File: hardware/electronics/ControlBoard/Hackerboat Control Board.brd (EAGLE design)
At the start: 177.8 x 114.3 mm, 178 parts, among them J3 3-1437664-0, U1 IPS6044, U14 TPS54331, U15 TPS54331, U2 ARDUINO-MEGAFULL, U3 IPS6044, U4 IPS6044, U5 IPS6044

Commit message: Added hardware test code Various modifications to 'as-built' condition Added TODO.md
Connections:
- net N$1 renamed GNSS_RX
- net N$2 renamed GNSS_TX
- net N$67 renamed SYS_5V
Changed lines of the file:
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@@
 <wire x1="54.61" y1="60.325" x2="56.515" y2="58.42" width="0.254" layer="1"/>
 </signal>
-<signal name="N$1">
+<signal name="GNSS_RX">
 <contactref element="GPS" pad="RX"/>
 <contactref element="U$1" pad="59"/>
@@
 <wire x1="57.785" y1="49.53" x2="59.055" y2="48.26" width="0.254" layer="16"/>
 </signal>
-<signal name="N$2">
+<signal name="GNSS_TX">
 <contactref element="GPS" pad="TX"/>
 <contactref element="U$1" pad="57"/>
@@
 <wire x1="59.055" y1="43.18" x2="63.373" y2="43.18" width="0.4064" layer="16"/>
 </signal>
-<signal name="N$67">
+<signal name="SYS_5V">
 <contactref element="GPS" pad="VIN"/>
 <contactref element="U$1" pad="53"/>

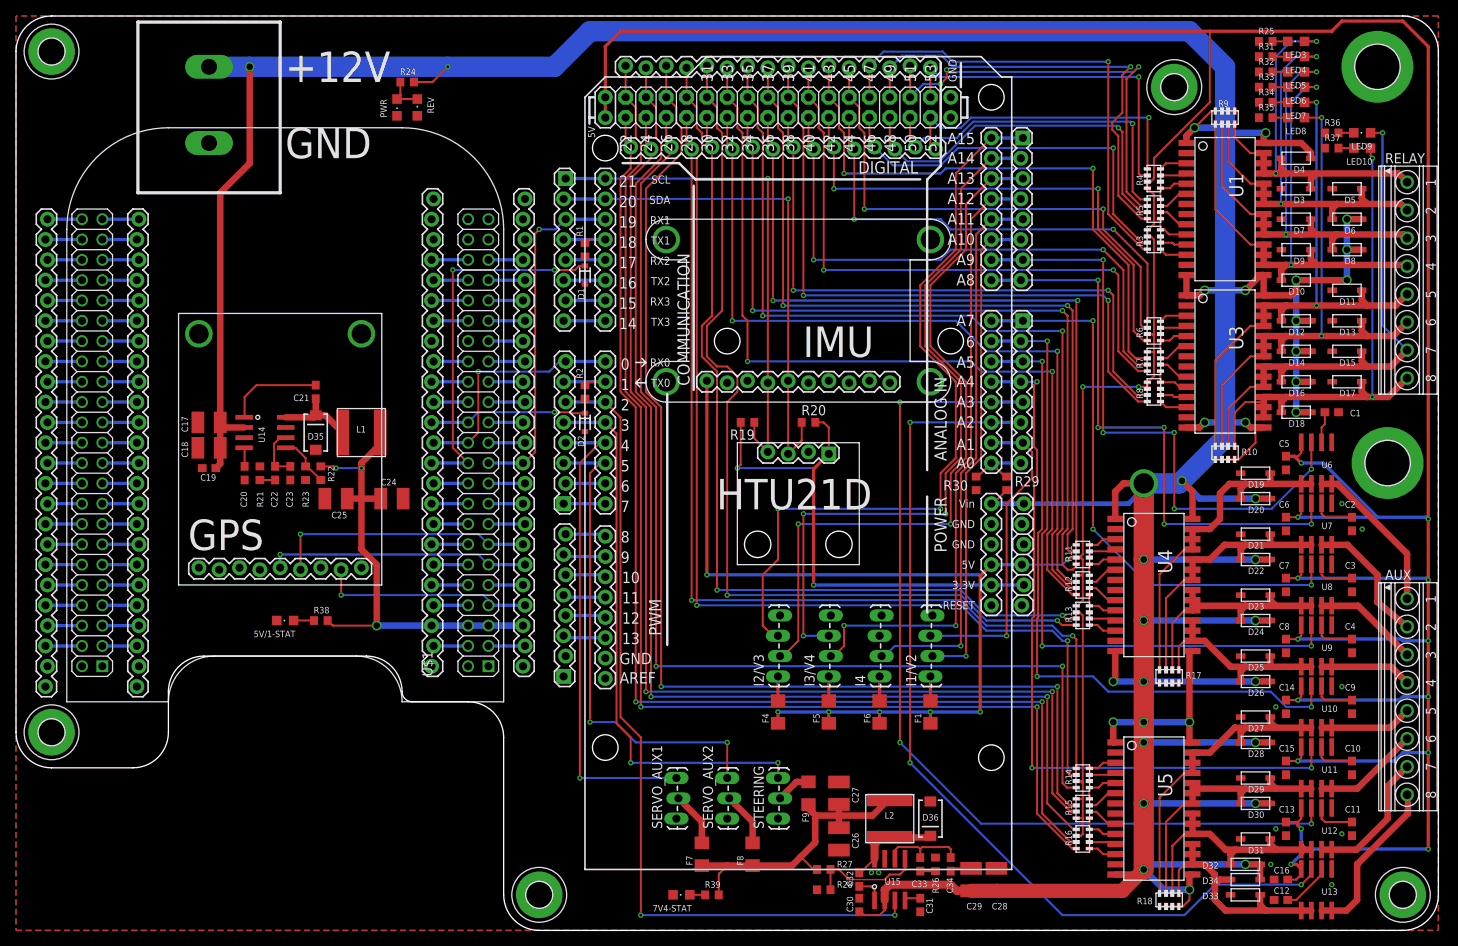
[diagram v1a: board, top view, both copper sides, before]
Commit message: Initial trimming of unnecessary parts in preparation for serious work. Keeping the power supply circuits, BBB connection, IMU, and GPS.
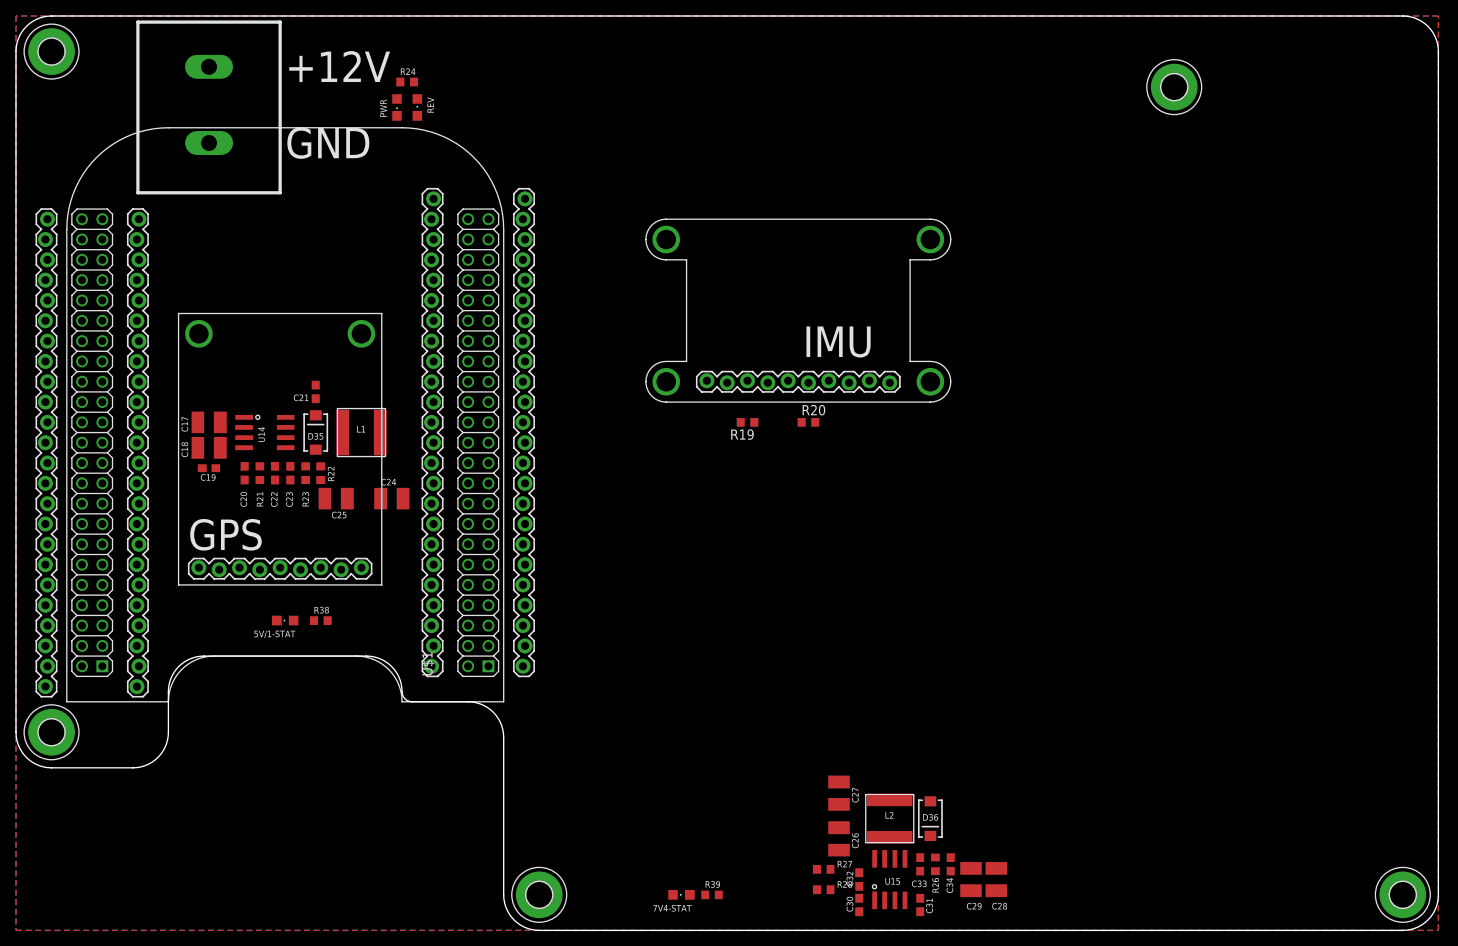
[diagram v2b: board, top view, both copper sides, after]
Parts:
- removed AUX, RELAY: 1751303, con-phoenix-350:1751303
- removed C1, C10, C11, C12, C2, C3, C4, C9: 1n, resistor:C0603
- removed C13, C14, C15, C16, C5, C6, C7, C8: 100n, resistor:C0603
- removed D1, D2: 3.3V, SparkFun-DiscreteSemi:SOD-323
- removed D10, D11, D12, D13, D14, D15, D16, D17, D18, D19, D20, D21, D22, D23, D24, D25, D26, D27, D28, D29, D3, D30, D31, D32, D33, D34, D4, D5, D6, D7, D8, D9: (no value), adafruit:SOD-123
- removed F1, F4, F5, F6, F7, F8, F9: (no value), adafruit:R1206
- removed H5, H6: MOUNT-PAD-ROUND5.5, holes:5,5-PAD
- removed HTU21D: HTU21D, sparkfun-sensor-boards:HTU21D
- removed I1/V2, I2/V3, I3/V4, I4: (no value), SparkFun-Connectors:1X04_LOCK_LONGPADS
- removed JP10, JP11, JP12, JP13, JP14: (no value), SparkFun-Connectors:1X08_LOCK
- removed JP15, JP16: M16LOCK, SparkFun-Connectors:1X16_LOCK
- removed JP17: (no value), SparkFun-Connectors:1X06_LOCK
- removed LED10, LED3, LED4, LED5, LED6, LED7, LED8, LED9: (no value), adafruit:CHIPLED_0805
- removed R1, R2: 1K, resistor:R0603
- removed R10, R17, R18, R9: 100K, res-cap-arrays:CTS742C083-RES
- removed R11, R12, R13, R14, R15, R16, R3, R5, R6, R7, R8: 10K, res-cap-arrays:CTS742C083-RES
- removed R25, R31, R32, R33, R34, R35, R36, R37: (no value), resistor:R0603
- removed R29: 15K, resistor:R0603
- removed R30: 10K, resistor:R0603
- removed R4: 10k, res-cap-arrays:CTS742C083-RES
- removed SERVO_AUX1, SERVO_AUX2, STEERING: (no value), SparkFun-Connectors:1X03_LOCK_LONGPADS
- removed U1, U3, U4, U5: IPS6044, logos-faves:SO-28L
- removed U10, U11, U12, U13, U6, U7, U8, U9: (no value), allegro3:SO08
- removed U2: ARDUINO-MEGAFULL, SparkFun-Boards:ARDUINO_MEGA
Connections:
- removed net +5V/1: C24.1, C25.1, L1.2, R22.2, R38.2, U$1.51, U$1.52, U$2.23, U$5.23
- removed net 13: JP14.3, U2.13
- removed net AUX1: JP15.9, R11.1, U2.36
- removed net AUX1FB: JP16.9, R11.3, U2.37
- removed net AUX1I: JP12.7, U2.A9, U6.7
- removed net AUX2: JP16.10, R12.3, U2.35
- removed net AUX2FB: JP15.10, R11.7, U2.34
- removed net AUX2I: JP12.8, U2.A8, U7.7
- removed net AUX3: JP15.11, R12.5, U2.32
- removed net AUX3FB: JP16.11, R12.7, U2.33
- removed net AUX3I: JP11.1, U2.A7, U8.7
- removed net AUX4: JP16.12, R13.7, U2.31
- removed net AUX4FB: JP15.12, R13.5, U2.30
- removed net AUX4I: JP11.2, U2.A6, U9.7
- removed net AUX5: JP15.13, R14.1, U2.28
- removed net AUX5FB: JP16.13, R14.3, U2.29
- removed net AUX5I: JP11.3, U10.7, U2.A5
- removed net AUX6: JP16.14, R15.3, U2.27
- removed net AUX6FB: JP15.14, R14.7, U2.26
- removed net AUX6I: JP11.4, U11.7, U2.A4
- removed net AUX7: JP15.15, R15.5, U2.24
- removed net AUX7FB: JP16.15, R16.1, U2.25
- removed net AUX7I: JP11.5, U12.7, U2.A3
- removed net AUX8: JP16.16, R16.7, U2.23
- removed net AUX8FB: JP15.16, R16.5, U2.22
- removed net AUX8I: JP11.6, U13.7, U2.A2
- removed net I1: I1/V2.2, JP12.6, U2.A10
- removed net I2: I2/V3.2, JP12.3, U2.A13
- removed net I3: I3/V4.2, JP12.4, U2.A12
- removed net I4: I4.2, JP12.5, U2.A11
- removed net N$10: D7.C, D8.A, LED5.A, R9.3, RELAY.3, U1.19, U1.20, U1.21
- removed net N$100: JP14.7, U2.9
- removed net N$101: JP14.6, U2.10
- removed net N$102: JP14.5, U2.11
- removed net N$103: JP14.4, U2.12
- removed net N$11: D10.A, D9.C, LED6.A, R9.1, RELAY.4, U1.16, U1.17, U1.18
- removed net N$12: R4.2, U1.3
- removed net N$13: R5.4, U1.6
- removed net N$14: R5.6, U1.9
- removed net N$15: R3.8, U1.12
- removed net N$16: R4.4, R4.6, U1.4
- removed net N$17: R4.8, R5.2, U1.5
- removed net N$178: LED3.C, R25.2
- removed net N$179: LED4.C, R31.2
- removed net N$18: R3.2, R5.8, U1.10
- removed net N$180: LED5.C, R32.2
- removed net N$181: LED6.C, R33.2
- removed net N$186: LED7.C, R34.2
- removed net N$187: LED8.C, R35.2
- removed net N$188: LED9.C, R36.2
- removed net N$189: LED10.C, R37.2
- removed net N$19: R3.4, R3.6, U1.11
- removed net N$20: R7.4, U3.6
- removed net N$21: R6.8, R7.2, U3.5
- removed net N$22: R6.4, R6.6, U3.4
- removed net N$23: R7.8, R8.2, U3.10
- removed net N$24: R8.4, R8.6, U3.11
- removed net N$25: D11.C, D12.A, LED7.A, R10.7, RELAY.5, U3.25, U3.26, U3.27
- removed net N$26: D13.C, D14.A, LED8.A, R10.5, RELAY.6, U3.22, U3.23, U3.24
- removed net N$27: D15.C, D16.A, LED9.A, R10.3, RELAY.7, U3.19, U3.20, U3.21
- removed net N$28: D17.C, D18.A, LED10.A, R10.1, RELAY.8, U3.16, U3.17, U3.18
- removed net N$29: D25.C, D26.A, R17.1, U4.16, U4.17, U4.18, U9.1, U9.2
- removed net N$3: JP13.4, R1.1, U2.18
- removed net N$30: AUX.2, U7.3, U7.4
- removed net N$31: AUX.3, U8.3, U8.4
- removed net N$32: AUX.4, U9.3, U9.4
- removed net N$33: AUX.5, U10.3, U10.4
- removed net N$34: D19.C, D20.A, R17.7, U4.25, U4.26, U4.27, U6.1, U6.2
- removed net N$35: D21.C, D22.A, R17.5, U4.22, U4.23, U4.24, U7.1, U7.2
- removed net N$36: D23.C, D24.A, R17.3, U4.19, U4.20, U4.21, U8.1, U8.2
- removed net N$37: AUX.1, U6.3, U6.4
- removed net N$38: R11.2, U4.3
- removed net N$39: R12.4, U4.6
- removed net N$4: JP10.7, R2.2, U2.1
- removed net N$40: R12.6, U4.9
- removed net N$41: R13.8, U4.12
- removed net N$42: R11.4, R11.6, U4.4
- removed net N$43: R11.8, R12.2, U4.5
- removed net N$44: R12.8, R13.2, U4.10
- removed net N$45: R13.4, R13.6, U4.11
- removed net N$46: R14.2, U5.3
- removed net N$47: R16.8, U5.12
- removed net N$48: R15.6, U5.9
- removed net N$49: R15.4, U5.6
- removed net N$5: R6.2, U3.3
- removed net N$50: R14.4, R14.6, U5.4
- removed net N$51: R14.8, R15.2, U5.5
- removed net N$52: R15.8, R16.2, U5.10
- removed net N$53: R16.4, R16.6, U5.11
- removed net N$54: D27.C, D28.A, R18.7, U10.1, U10.2, U5.25, U5.26, U5.27
- removed net N$55: D29.C, D30.A, R18.5, U11.1, U11.2, U5.22, U5.23, U5.24
- removed net N$56: D31.C, D32.A, R18.3, U12.1, U12.2, U5.19, U5.20, U5.21
- removed net N$57: D33.C, D34.A, R18.1, U13.1, U13.2, U5.16, U5.17, U5.18
- removed net N$58: AUX.6, U11.3, U11.4
- removed net N$59: AUX.7, U12.3, U12.4
- removed net N$6: R8.8, U3.12
- removed net N$60: AUX.8, U13.3, U13.4
- removed net N$61: C1.2, U6.6
- removed net N$64: C2.2, U7.6
- removed net N$65: C3.2, U8.6
- removed net N$66: C4.2, U9.6
- removed net N$7: R7.6, U3.9
- removed net N$74: C9.2, U10.6
- removed net N$75: C10.2, U11.6
- removed net N$76: C11.2, U12.6
- removed net N$77: C12.2, U13.6
- removed net N$8: D3.C, D4.A, LED3.A, R9.7, RELAY.1, U1.25, U1.26, U1.27
- removed net N$83: F1.2, I1/V2.1
- removed net N$86: F4.2, I2/V3.1
- removed net N$87: F5.2, I3/V4.1
- removed net N$88: F6.2, I4.1
- removed net N$89: F7.2, SERVO_AUX1.2
- removed net N$9: D5.C, D6.A, LED4.A, R9.5, RELAY.2, U1.22, U1.23, U1.24
- removed net N$90: F8.2, SERVO_AUX2.2
- removed net N$91: JP10.1, U2.7
- removed net N$92: JP10.2, U2.6
- removed net N$93: F9.2, STEERING.2
- removed net N$94: JP11.8, R29.1, R30.2, U2.A0
- removed net N$95: JP13.5, U2.17
- removed net N$96: JP13.6, U2.16
- removed net N$97: JP13.7, U2.15
- removed net N$98: JP13.8, U2.14
- removed net N$99: JP14.8, U2.8
- removed net RELAY1: JP15.1, R4.1, U2.52
- removed net RELAY1FB: JP16.1, R4.3, U2.53
- removed net RELAY2: JP16.2, R5.3, U2.51
- removed net RELAY2FB: JP15.2, R5.1, U2.50
- removed net RELAY3: JP15.3, R5.5, U2.48
- removed net RELAY3FB: JP16.3, R5.7, U2.49
- removed net RELAY4: JP16.4, R3.7, U2.47
- removed net RELAY4FB: JP15.4, R3.5, U2.46
- removed net RELAY5: JP15.5, R6.1, U2.44
- removed net RELAY5FB: JP16.5, R6.3, U2.45
- removed net RELAY6: JP16.6, R7.3, U2.43
- removed net RELAY6FB: JP15.6, R6.7, U2.42
- removed net RELAY7: JP15.7, R7.5, U2.40
- removed net RELAY7FB: JP16.7, R7.7, U2.41
- removed net RELAY8: JP16.8, R8.7, U2.39
- removed net RELAY8FB: JP15.8, R8.5, U2.38
- removed net SCL: HTU21D.SCL, IMU.SCL, JP13.1, R19.1, U2.21
- removed net SDA: HTU21D.SDA, IMU.SDA, JP13.2, R20.1, U2.20
- removed net SERVO_AUX1: JP10.4, SERVO_AUX1.3, U2.4
- removed net SERVO_AUX2: JP10.3, SERVO_AUX2.3, U2.5
- removed net STEERING: JP10.5, STEERING.3, U2.3
- removed net V2: I1/V2.3, JP11.7, U2.A1
- removed net V3: I2/V3.3, JP12.1, U2.A15
- removed net V4: I3/V4.3, JP12.2, U2.A14
- new net N$196: IMU.SDA, R20.1
- new net N$197: IMU.SCL, R19.1
- net +12V: no longer D10.C, D12.C, D14.C, D16.C, D18.C, D20.C, D22.C, D24.C, D26.C, D28.C, D30.C, D32.C, D34.C, D4.C, D6.C, D8.C, JP17.6, R10.2, R10.4, R10.6, R10.8, R17.2, R17.4, R17.6, R17.8, R18.2, R18.4, R18.6, R18.8, R29.2, R9.2, R9.4, R9.6, R9.8, U1.1, U1.14, U1.15, U1.28, U2.VIN, U3.1, U3.14, U3.15, U3.28, U4.1, U4.14, U4.15, U4.28, U5.1, U5.14, U5.15, U5.28
- net +3V3: no longer HTU21D.3V3, JP17.2, U2.3.3V
- net +5V: now also C24.1, C25.1, L1.2, R22.2, R38.2, U$1.51, U$1.52, U$2.23, U$5.23; no longer C13.2, C14.2, C15.2, C16.2, C5.2, C6.2, C7.2, C8.2, F1.1, F4.1, F5.1, F6.1, JP17.3, R11.5, R12.1, R13.1, R13.3, R14.5, R15.1, R15.7, R16.3, R3.1, R3.3, R4.5, R4.7, R6.5, R7.1, R8.1, R8.3, U10.8, U11.8, U12.8, U13.8, U2.5V@0, U2.5V@1, U2.5V@2, U6.8, U7.8, U8.8, U9.8
- net 7V4: no longer F7.1, F8.1, F9.1
- net GND: no longer C1.1, C10.1, C11.1, C12.1, C13.1, C14.1, C15.1, C16.1, C2.1, C3.1, C4.1, C5.1, C6.1, C7.1, C8.1, C9.1, D1.A, D11.A, D13.A, D15.A, D17.A, D19.A, D2.A, D21.A, D23.A, D25.A, D27.A, D29.A, D3.A, D31.A, D33.A, D5.A, D7.A, D9.A, H5.B5,5, H6.B5,5, HTU21D.GND, I1/V2.4, I2/V3.4, I3/V4.4, I4.4, JP17.4, JP17.5, R25.1, R30.1, R31.1, R32.1, R33.1, R34.1, R35.1, R36.1, R37.1, SERVO_AUX1.1, SERVO_AUX2.1, STEERING.1, U1.13, U1.2, U1.7, U1.8, U10.5, U11.5, U12.5, U13.5, U2.GND@0, U2.GND@1, U2.GND@2, U2.GND@3, U2.GND@4, U3.13, U3.2, U3.7, U3.8, U4.13, U4.2, U4.7, U4.8, U5.13, U5.2, U5.7, U5.8, U6.5, U7.5, U8.5, U9.5
- net RX0: no longer JP10.8, U2.0
- net RX1: no longer JP13.3, U2.19
- net SERVO_EN: no longer JP10.6, U2.2
- net TX0: no longer D2.C, R2.1
- net TX1: no longer D1.C, R1.2
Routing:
- net +12V: track 644.3 -> 0.00 mm, vias 36 -> 0
- net +5V: track 604.3 -> 0.00 mm, vias 23 -> 0
- net AUX8: track 152.1 -> 0.00 mm, vias 2 -> 0
- net AUX7FB: track 149.4 -> 0.00 mm, vias 2 -> 0
- net AUX6: track 146.9 -> 0.00 mm, vias 2 -> 0
- net AUX8FB: track 145.1 -> 0.00 mm, vias 2 -> 0
- net AUX7: track 141.3 -> 0.00 mm, vias 2 -> 0
- net AUX6FB: track 138.6 -> 0.00 mm, vias 2 -> 0
- net AUX5FB: track 134.1 -> 0.00 mm, vias 2 -> 0
- net AUX5: track 126.8 -> 0.00 mm, vias 2 -> 0
- net AUX8I: track 117.2 -> 0.00 mm, vias 3 -> 0
- net AUX4: track 115.8 -> 0.00 mm, vias 2 -> 0
- net AUX7I: track 115.5 -> 0.00 mm, vias 3 -> 0
- net AUX4FB: track 107.0 -> 0.00 mm, vias 2 -> 0
- net AUX3FB: track 106.3 -> 0.00 mm, vias 2 -> 0
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
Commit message: First cut at the system block diagram
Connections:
- removed net N$118: U$1.50, U$2.24
- removed net N$71: U$1.49, U$5.24
- net +3V3: now also U$1.49, U$1.50, U$2.24, U$5.24
- net GND: no longer GPS.GND
- net GNSS_RX: no longer GPS.RX
- net GNSS_TX: no longer GPS.TX
- net SYS_5V: no longer GPS.VIN
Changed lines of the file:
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@@
 <contactref element="U$1" pad="91"/>
 <contactref element="U$1" pad="89"/>
-<contactref element="U$1" pad="92"/>
 <contactref element="U$1" pad="90"/>
-<contactref element="U$1" pad="2"/>
-<contactref element="U$1" pad="48"/>
-<contactref element="U$1" pad="80"/>
 <contactref element="IMU" pad="GND"/>
 <contactref element="H1" pad="B3,2"/>
@@
 <contactref element="C27" pad="2"/>
 <contactref element="R28" pad="1"/>
-<contactref element="U$2" pad="3"/>
 <contactref element="U$2" pad="4"/>
-<contactref element="U$2" pad="9"/>
-<contactref element="U$2" pad="25"/>
-<contactref element="U$3" pad="24"/>
 <contactref element="U$5" pad="4"/>
 <contactref element="J3" pad="2"/>
@@
 <contactref element="U$1" pad="1"/>
 <contactref element="U$1" pad="47"/>
-<contactref element="GPS" pad="GND"/>
 <contactref element="U$4" pad="24"/>
 <contactref element="U$5" pad="25"/>
@@
 <contactref element="7V4-STAT" pad="C"/>
 <contactref element="H7" pad="B3,2"/>
+<contactref element="U$1" pad="92"/>
+<contactref element="U$1" pad="92"/>
+<contactref element="U$2" pad="3"/>
+<contactref element="U$1" pad="2"/>
+<contactref element="U$1" pad="48"/>
+<contactref element="U$2" pad="25"/>
+<contactref element="U$3" pad="24"/>
+<contactref element="U$1" pad="80"/>
+<contactref element="U$2" pad="9"/>
 <wire x1="114.3" y1="86.36" x2="144.78" y2="105.41" width="0" layer="19" extent="1-1"/>
 <wire x1="114.3" y1="68.58" x2="114.3" y2="86.36" width="0" layer="19" extent="1-1"/>
@@
 <wire x1="22.73" y1="60.325" x2="23.28" y2="57.785" width="0" layer="19" extent="1-1"/>
 <wire x1="22.73" y1="63.5" x2="22.73" y2="60.325" width="0" layer="19" extent="1-1"/>
-<wire x1="38.1" y1="45.339" x2="38.605" y2="53.975" width="0" layer="19" extent="1-1"/>
-<wire x1="32.605" y1="38.735" x2="38.1" y2="45.339" width="0" layer="19" extent="1-1"/>
 <wire x1="48.39" y1="53.975" x2="38.605" y2="53.975" width="0" layer="19" extent="1-1"/>
 <wire x1="22.86" y1="74.5744" x2="22.73" y2="63.5" width="0" layer="19" extent="1-1"/>
+<wire x1="32.605" y1="38.735" x2="38.605" y2="53.975" width="0" layer="19" extent="1-1"/>
 <wire x1="15.367" y1="33.02" x2="32.605" y2="38.735" width="0" layer="19" extent="1-1"/>
 <wire x1="10.795" y1="33.02" x2="15.367" y2="33.02" width="0" layer="19" extent="1-1"/>
@@
 <wire x1="3.937" y1="33.02" x2="8.255" y2="33.02" width="0" layer="19" extent="1-1"/>
 <wire x1="4.445" y1="24.765" x2="3.937" y2="33.02" width="0" layer="19" extent="1-1"/>
-<wire x1="51.943" y1="33.02" x2="38.1" y2="45.339" width="0" layer="19" extent="1-1"/>
+<wire x1="51.943" y1="33.02" x2="32.605" y2="38.735" width="0" layer="19" extent="1-1"/>
 <wire x1="56.515" y1="33.02" x2="51.943" y2="33.02" width="0" layer="19" extent="1-1"/>
 <wire x1="59.055" y1="33.02" x2="56.515" y2="33.02" width="0" layer="19" extent="1-1"/>
@@
 </signal>
 <signal name="GNSS_RX">
-<contactref element="GPS" pad="RX"/>
 <contactref element="U$1" pad="59"/>
 <contactref element="U$5" pad="19"/>
 <wire x1="59.055" y1="48.26" x2="63.373" y2="48.26" width="0" layer="19" extent="1-1"/>
-<wire x1="35.56" y1="45.085" x2="59.055" y2="48.26" width="0" layer="19" extent="1-1"/>
 </signal>
 <signal name="GNSS_TX">
-<contactref element="GPS" pad="TX"/>
 <contactref element="U$1" pad="57"/>
 <contactref element="U$5" pad="20"/>
 <wire x1="59.055" y1="45.72" x2="63.627" y2="45.72" width="0" layer="19" extent="1-1"/>
-<wire x1="33.02" y1="45.339" x2="59.055" y2="45.72" width="0" layer="19" extent="1-1"/>
 </signal>
 <signal name="+3V3">
 <contactref element="R19" pad="2"/>
 <contactref element="R20" pad="2"/>
+<contactref element="U$1" pad="49"/>
+<contactref element="U$5" pad="24"/>
+<contactref element="U$1" pad="50"/>
+<contactref element="U$2" pad="24"/>
 <wire x1="90.59" y1="63.5" x2="99.91" y2="63.5" width="0" layer="19" extent="1-1"/>
+<wire x1="63.627" y1="35.56" x2="90.59" y2="63.5" width="0" layer="19" extent="1-1"/>
+<wire x1="59.055" y1="35.56" x2="63.627" y2="35.56" width="0" layer="19" extent="1-1"/>
+<wire x1="56.515" y1="35.56" x2="59.055" y2="35.56" width="0" layer="19" extent="1-1"/>
+<wire x1="52.197" y1="35.56" x2="56.515" y2="35.56" width="0" layer="19" extent="1-1"/>
 </signal>
 <signal name="+5V">
@@
 <wire x1="52.197" y1="40.64" x2="56.515" y2="40.64" width="0" layer="19" extent="1-1"/>
 </signal>
-<signal name="N$118">
-<contactref element="U$1" pad="50"/>
-<contactref element="U$2" pad="24"/>
-<wire x1="52.197" y1="35.56" x2="56.515" y2="35.56" width="0" layer="19" extent="1-1"/>
-</signal>
 <signal name="N$119">
 <contactref element="U$1" pad="46"/>
@@
 </signal>
 <signal name="SYS_5V">
-<contactref element="GPS" pad="VIN"/>
 <contactref element="U$1" pad="53"/>
 <contactref element="U$5" pad="22"/>
 <wire x1="59.055" y1="40.64" x2="63.627" y2="40.64" width="0" layer="19" extent="1-1"/>
-<wire x1="40.64" y1="45.085" x2="59.055" y2="40.64" width="0" layer="19" extent="1-1"/>
-</signal>
-<signal name="N$71">
-<contactref element="U$1" pad="49"/>
-<contactref element="U$5" pad="24"/>
-<wire x1="59.055" y1="35.56" x2="63.627" y2="35.56" width="0" layer="19" extent="1-1"/>
 </signal>
 <signal name="N$177">
